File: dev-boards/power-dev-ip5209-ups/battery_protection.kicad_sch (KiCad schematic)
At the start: 3 parts, among them U2 XB5350D0

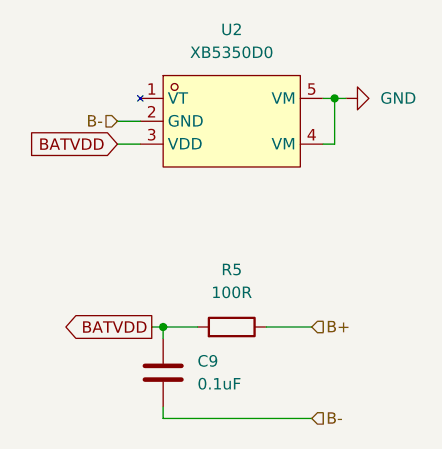
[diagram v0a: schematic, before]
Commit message: Replace XB5350D0 with XB3306D for battery protection
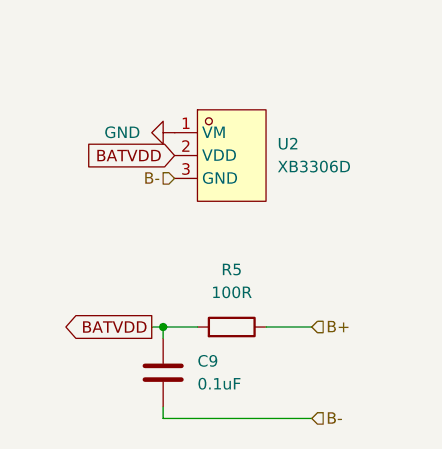
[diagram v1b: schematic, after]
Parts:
- removed U2: XB5350D0, custom:SOT-23-5_simple, symbol lcsc:XB5350D0
- added U2: XB3306D, Package_TO_SOT_SMD:SOT-23-3, symbol lcsc:XB3306D
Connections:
- net B-: now also U2.3 (GND)
- net BATVDD: now also U2.2 (VDD)
- net GND: now also U2.1 (VM)
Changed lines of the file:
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@@
 		(color 0 0 0 0)
 	)
-	(junction
-		(at 158.75 78.74)
-		(diameter 0)
-		(color 0 0 0 0)
-	)
 	(wire
 		(pts
@@
 	(wire
 		(pts
-			(xy 158.75 78.74) (xy 157.48 78.74)
-		)
-		(stroke
-			(width 0)
-			(type default)
-		)
-	)
-	(wire
-		(pts
 			(xy 138.43 104.14) (xy 139.7 104.14)
 		)
@@
 	(wire
 		(pts
-			(xy 160.02 78.74) (xy 158.75 78.74)
-		)
-		(stroke
-			(width 0)
-			(type default)
-		)
-	)
-	(wire
-		(pts
 			(xy 143.51 104.14) (xy 139.7 104.14)
 		)
@@
 	(wire
 		(pts
-			(xy 158.75 83.82) (xy 158.75 78.74)
-		)
-		(stroke
-			(width 0)
-			(type default)
-		)
-	)
-	(wire
-		(pts
-			(xy 134.62 81.28) (xy 137.16 81.28)
-		)
-		(stroke
-			(width 0)
-			(type default)
-		)
-	)
-	(wire
-		(pts
 			(xy 139.7 114.3) (xy 156.21 114.3)
 		)
@@
 	(wire
 		(pts
-			(xy 134.62 83.82) (xy 137.16 83.82)
-		)
-		(stroke
-			(width 0)
-			(type default)
-		)
-	)
-	(wire
-		(pts
 			(xy 139.7 104.14) (xy 139.7 105.41)
-		)
-		(stroke
-			(width 0)
-			(type default)
-		)
-	)
-	(wire
-		(pts
-			(xy 157.48 83.82) (xy 158.75 83.82)
 		)
 		(stroke
@@
 	(global_label "BATVDD"
 		(shape input)
-		(at 134.62 83.82 180)
+		(at 140.97 85.09 180)
 		(fields_autoplaced yes)
 		(effects
@@
 		)
 		(property "Intersheetrefs" "${INTERSHEET_REFS}"
-			(at 124.68 83.82 0)
+			(at 131.03 85.09 0)
 			(effects
 				(font
@@
 	(hierarchical_label "B-"
 		(shape input)
-		(at 134.62 81.28 180)
+		(at 156.21 114.3 0)
 		(fields_autoplaced yes)
 		(effects
@@
 				(size 1.27 1.27)
 			)
-			(justify right)
-		)
-	)
-	(hierarchical_label "B-"
+			(justify left)
+		)
+	)
+	(hierarchical_label "B+"
 		(shape input)
-		(at 156.21 114.3 0)
+		(at 156.21 104.14 0)
 		(fields_autoplaced yes)
 		(effects
@@
 		)
 	)
-	(hierarchical_label "B+"
+	(hierarchical_label "B-"
 		(shape input)
-		(at 156.21 104.14 0)
+		(at 140.97 87.63 180)
 		(fields_autoplaced yes)
 		(effects
@@
 				(size 1.27 1.27)
 			)
-			(justify left)
+			(justify right)
 		)
 	)
 	(symbol
-		(lib_id "lcsc:XB5350D0")
-		(at 147.32 81.28 0)
+		(lib_id "power:GND")
+		(at 140.97 82.55 270)
 		(unit 1)
 		(exclude_from_sim no)
@@
 		(dnp no)
 		(fields_autoplaced yes)
-		(property "Reference" "U2"
-			(at 147.32 71.12 0)
-			(effects
-				(font
-					(size 1.27 1.27)
-				)
-			)
-		)
-		(property "Value" "XB5350D0"
-			(at 147.32 73.66 0)
-			(effects
-				(font
-					(size 1.27 1.27)
-				)
-			)
-		)
-		(property "Footprint" "custom:SOT-23-5_simple"
-			(at 147.32 91.44 0)
-			(effects
-				(font
-					(size 1.27 1.27)
-				)
-				(hide yes)
-			)
-		)
-		(property "Datasheet" "https://www.lcsc.com/datasheet/lcsc_datasheet_2106062205_XySemi-XB5350D0_C2760002.pdf"
-			(at 147.32 81.28 0)
-			(effects
-				(font
-					(size 1.27 1.27)
-				)
-				(hide yes)
-			)
-		)
-		(property "Description" ""
-			(at 147.32 81.28 0)
-			(effects
-				(font
-					(size 1.27 1.27)
-				)
-				(hide yes)
-			)
-		)
-		(property "JLCPCB_CORRECTION" "0; 0; 180"
-			(at 147.32 81.28 0)
-			(effects
-				(font
-					(size 1.27 1.27)
-				)
-				(hide yes)
-			)
-		)
-		(property "LCSC Part" "C2760002"
-			(at 147.32 93.98 0)
-			(effects
-				(font
-					(size 1.27 1.27)
-				)
-				(hide yes)
-			)
-		)
-		(pin "4"
-		)
-		(pin "2"
+		(property "Reference" "#PWR030"
+			(at 134.62 82.55 0)
+			(effects
+				(font
+					(size 1.27 1.27)
+				)
+				(hide yes)
+			)
+		)
+		(property "Value" "GND"
+			(at 137.16 82.5499 90)
+			(effects
+				(font
+					(size 1.27 1.27)
+				)
+				(justify right)
+			)
+		)
+		(property "Footprint" ""
+			(at 140.97 82.55 0)
+			(effects
+				(font
+					(size 1.27 1.27)
+				)
+				(hide yes)
+			)
+		)
+		(property "Datasheet" ""
+			(at 140.97 82.55 0)
+			(effects
+				(font
+					(size 1.27 1.27)
+				)
+				(hide yes)
+			)
+		)
+		(property "Description" "Power symbol creates a global label with name \"GND\" , ground"
+			(at 140.97 82.55 0)
+			(effects
+				(font
+					(size 1.27 1.27)
+				)
+				(hide yes)
+			)
 		)
 		(pin "1"
 		)
-		(pin "3"
-		)
-		(pin "5"
-		)
 		(instances
-			(project "power-dev-ip5306-ups"
+			(project "power-dev-ip5209-ups"
 				(path "/76a56607-25e2-40a3-9282-ff279b153f75/7ff8b12e-1c69-42b0-a172-ea1bc26ada19"
-					(reference "U2")
+					(reference "#PWR030")
 					(unit 1)
 				)
@@
 	)
 	(symbol
-		(lib_id "power:GND")
-		(at 160.02 78.74 90)
-		(unit 1)
-		(exclude_from_sim no)
-		(in_bom yes)
-		(on_board yes)
-		(dnp no)
-		(fields_autoplaced yes)
-		(property "Reference" "#PWR03"
-			(at 166.37 78.74 0)
-			(effects
-				(font
-					(size 1.27 1.27)
-				)
-				(hide yes)
-			)
-		)
-		(property "Value" "GND"
-			(at 163.83 78.7399 90)
-			(effects
-				(font
-					(size 1.27 1.27)
-				)
-				(justify right)
-			)
-		)
-		(property "Footprint" ""
-			(at 160.02 78.74 0)
-			(effects
-				(font
-					(size 1.27 1.27)
-				)
-				(hide yes)
-			)
-		)
-		(property "Datasheet" ""
-			(at 160.02 78.74 0)
-			(effects
-				(font
-					(size 1.27 1.27)
-				)
-				(hide yes)
-			)
-		)
-		(property "Description" "Power symbol creates a global label with name \"GND\" , ground"
-			(at 160.02 78.74 0)
-			(effects
-				(font
-					(size 1.27 1.27)
-				)
-				(hide yes)
-			)
-		)
-		(pin "1"
-		)
-		(instances
-			(project "power-dev-ip5306-ups"
-				(path "/76a56607-25e2-40a3-9282-ff279b153f75/7ff8b12e-1c69-42b0-a172-ea1bc26ada19"
-					(reference "#PWR03")
-					(unit 1)
-				)
-			)
-		)
-	)
-	(symbol
 		(lib_id "Device:C")
 		(at 139.7 109.22 180)
@@
 					(unit 1)
 				)
+			)
+		)
+	)
+	(symbol
+		(lib_id "lcsc:XB3306D")
+		(at 147.32 85.09 0)
+		(unit 1)
+		(exclude_from_sim no)
+		(in_bom yes)
+		(on_board yes)
+		(dnp no)
+		(fields_autoplaced yes)
+		(property "Reference" "U2"
+			(at 152.4 83.8199 0)
+			(effects
+				(font
+					(size 1.27 1.27)
+				)
+				(justify left)
+			)
+		)
+		(property "Value" "XB3306D"
+			(at 152.4 86.3599 0)
+			(effects
+				(font
+					(size 1.27 1.27)
+				)
+				(justify left)
+			)
+		)
+		(property "Footprint" "Package_TO_SOT_SMD:SOT-23-3"
+			(at 147.32 95.25 0)
+			(effects
+				(font
+					(size 1.27 1.27)
+				)
+				(hide yes)
+			)
+		)
+		(property "Datasheet" ""
+			(at 147.32 85.09 0)
+			(effects
+				(font
+					(size 1.27 1.27)
+				)
+				(hide yes)
+			)
+		)
+		(property "Description" ""
+			(at 147.32 85.09 0)
+			(effects
+				(font
+					(size 1.27 1.27)
+				)
+				(hide yes)
+			)
+		)
+		(property "LCSC Part" "C2759992"
+			(at 147.32 97.79 0)
+			(effects
+				(font
+					(size 1.27 1.27)
+				)
+				(hide yes)
+			)
+		)
+		(pin "3"
+		)
+		(pin "1"
+		)
+		(pin "2"
+		)
+		(instances
+			(project ""
+				(path "/76a56607-25e2-40a3-9282-ff279b153f75/7ff8b12e-1c69-42b0-a172-ea1bc26ada19"
+					(reference "U2")
+					(unit 1)
+				)
